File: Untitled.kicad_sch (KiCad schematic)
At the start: 11 parts, among them K1 Fujitsu_FTR-LYAA005x, Q2 IRLB8721PBF, Q3 IRLB8721PBF, Q4 IRLB8721PBF, U1 ESP32-S3, U3 LSM6DS3, U4 MS5611-01BA

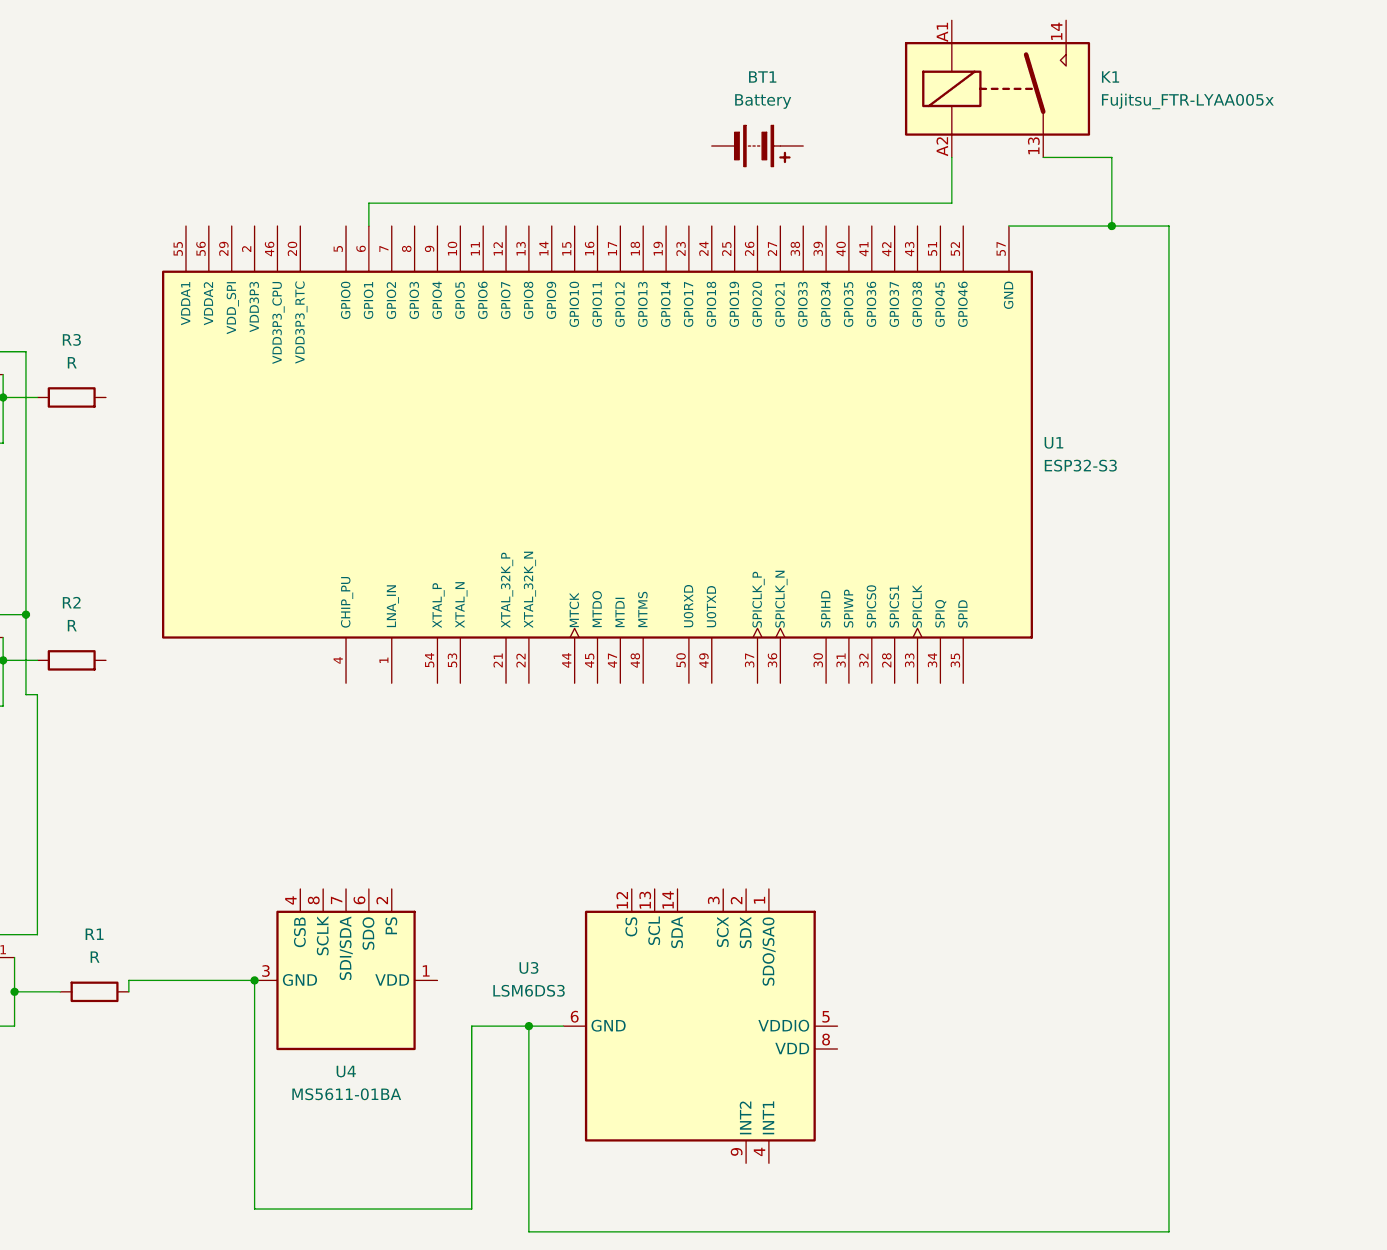
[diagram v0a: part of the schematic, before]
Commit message: Added Correct Microcontroller
Add the correct symbol for the microcontroller library
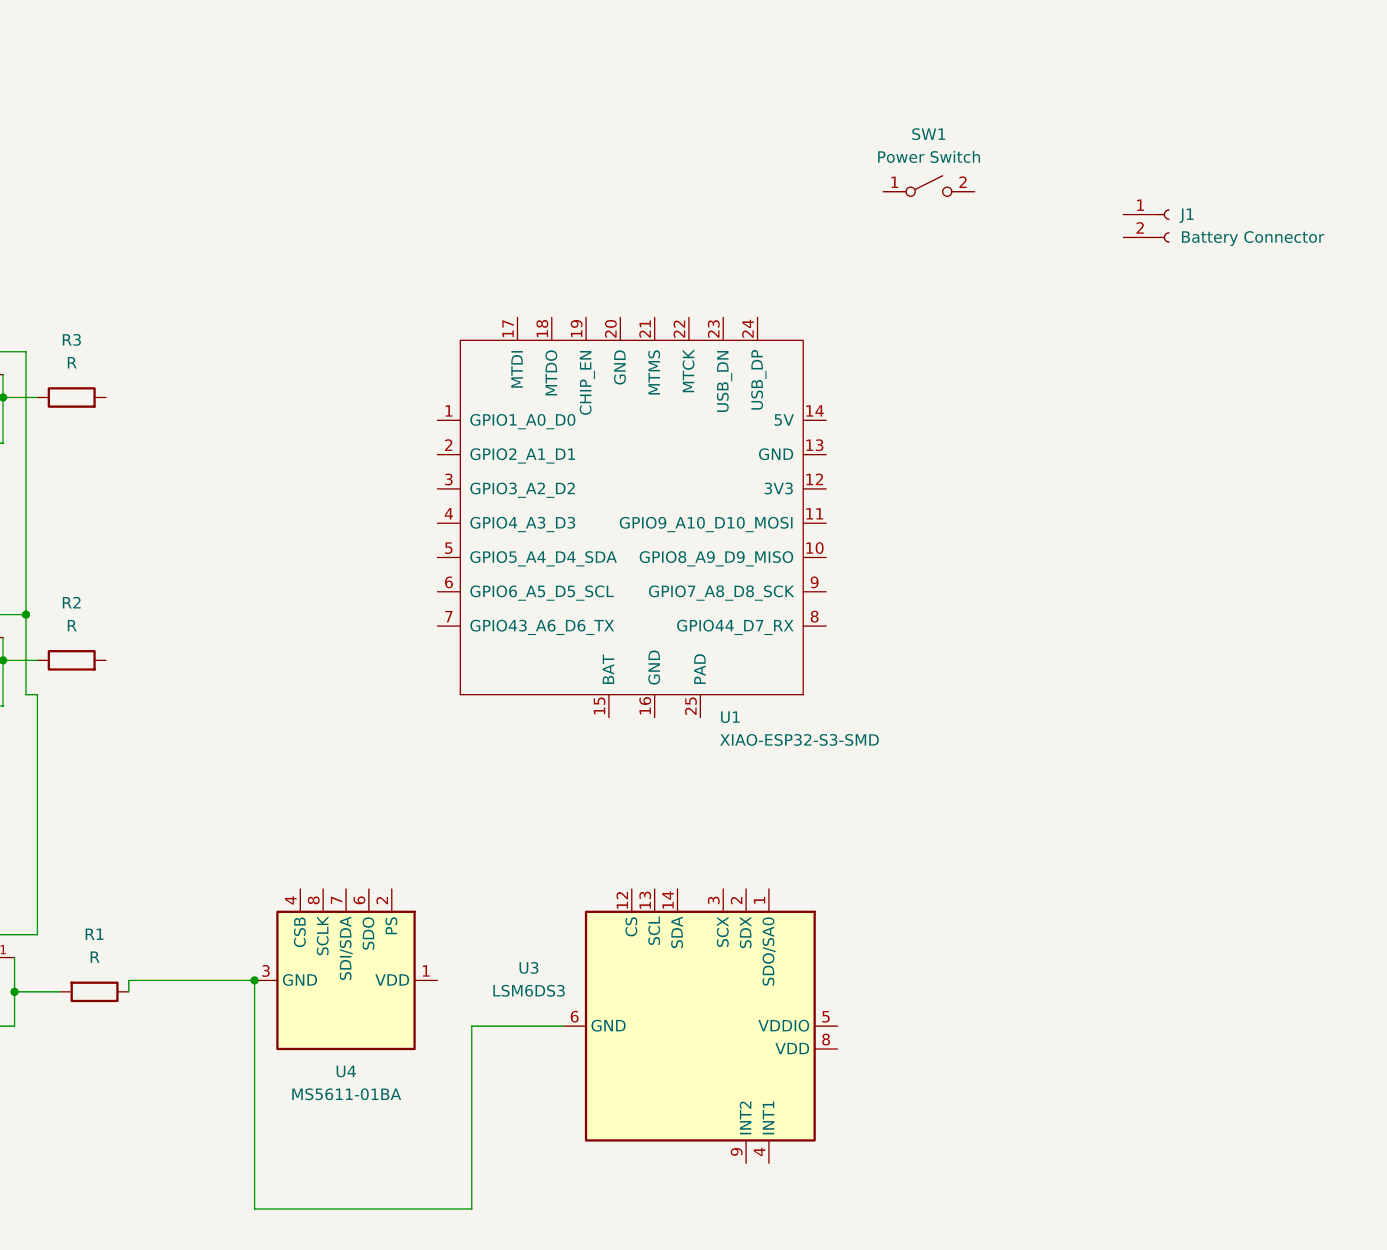
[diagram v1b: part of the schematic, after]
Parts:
- removed BT1: Battery, symbol Device:Battery
- removed K1: Fujitsu_FTR-LYAA005x, Relay_THT:Relay_SPST-NO_Fujitsu_FTR-LYAA005x_FormA_Vertical, symbol Relay:Fujitsu_FTR-LYAA005x
- removed U1: ESP32-S3, ESP32-S3:IC_ESP32-S3, symbol ESP32-S3:ESP32-S3
- added J1: Battery Connector, symbol Connector:Conn_01x02_Socket
- added SW1: Power Switch, symbol Switch:SW_SPST
- added U1: XIAO-ESP32-S3-SMD, symbol SeeedStudio-XIAO:XIAO-ESP32-S3-SMD

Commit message: Fixed Microcontroller Library
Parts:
- added C1, C2, C3: 100nF, symbol Device:C_US
- added R4, R5: 10K, symbol Device:R_US
- U1: footprint (none) -> Seeed Studio XIAO Series Library:XIAO-ESP32S3-DIP
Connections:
- net at U4.1 (VDD): now also U1.12 (3V3), U3.5 (VDDIO), U3.8 (VDD), U4.2 (PS), C1.1, C2.2, C3.1, R4.1, R5.1
- net at R1.1, U3.6 (GND), U3.7 (GND)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: now also U1.13 (GND), C1.2, C2.1, C3.2
- net at U4.7 (SDI/SDA): now also U1.5 (GPIO5_A4_D4_SDA), R4.2
- net at U4.8 (SCLK): now also U1.6 (GPIO6_A5_D5_SCL), R5.2

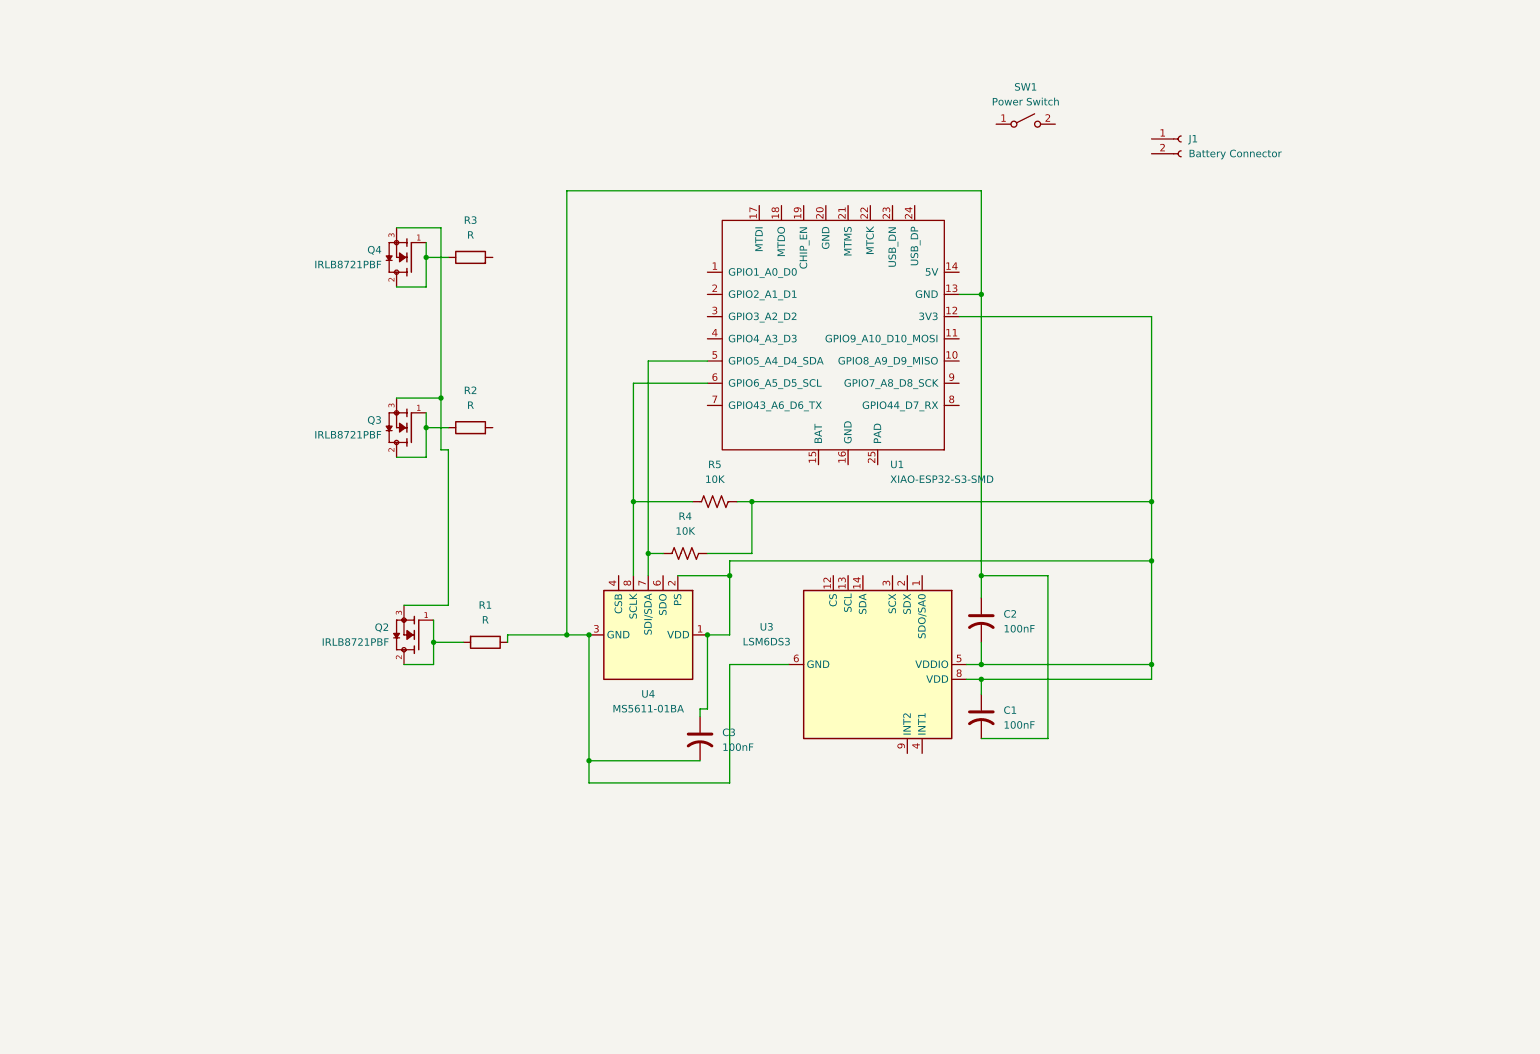
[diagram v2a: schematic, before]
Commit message: Sensor Wiring Finished
Finished the wiring for both sensors. Cleaned up diagram by using net labels rather than directly connecting everything. Left MOSTFETs unfinished bc they will likely be on a separate board.
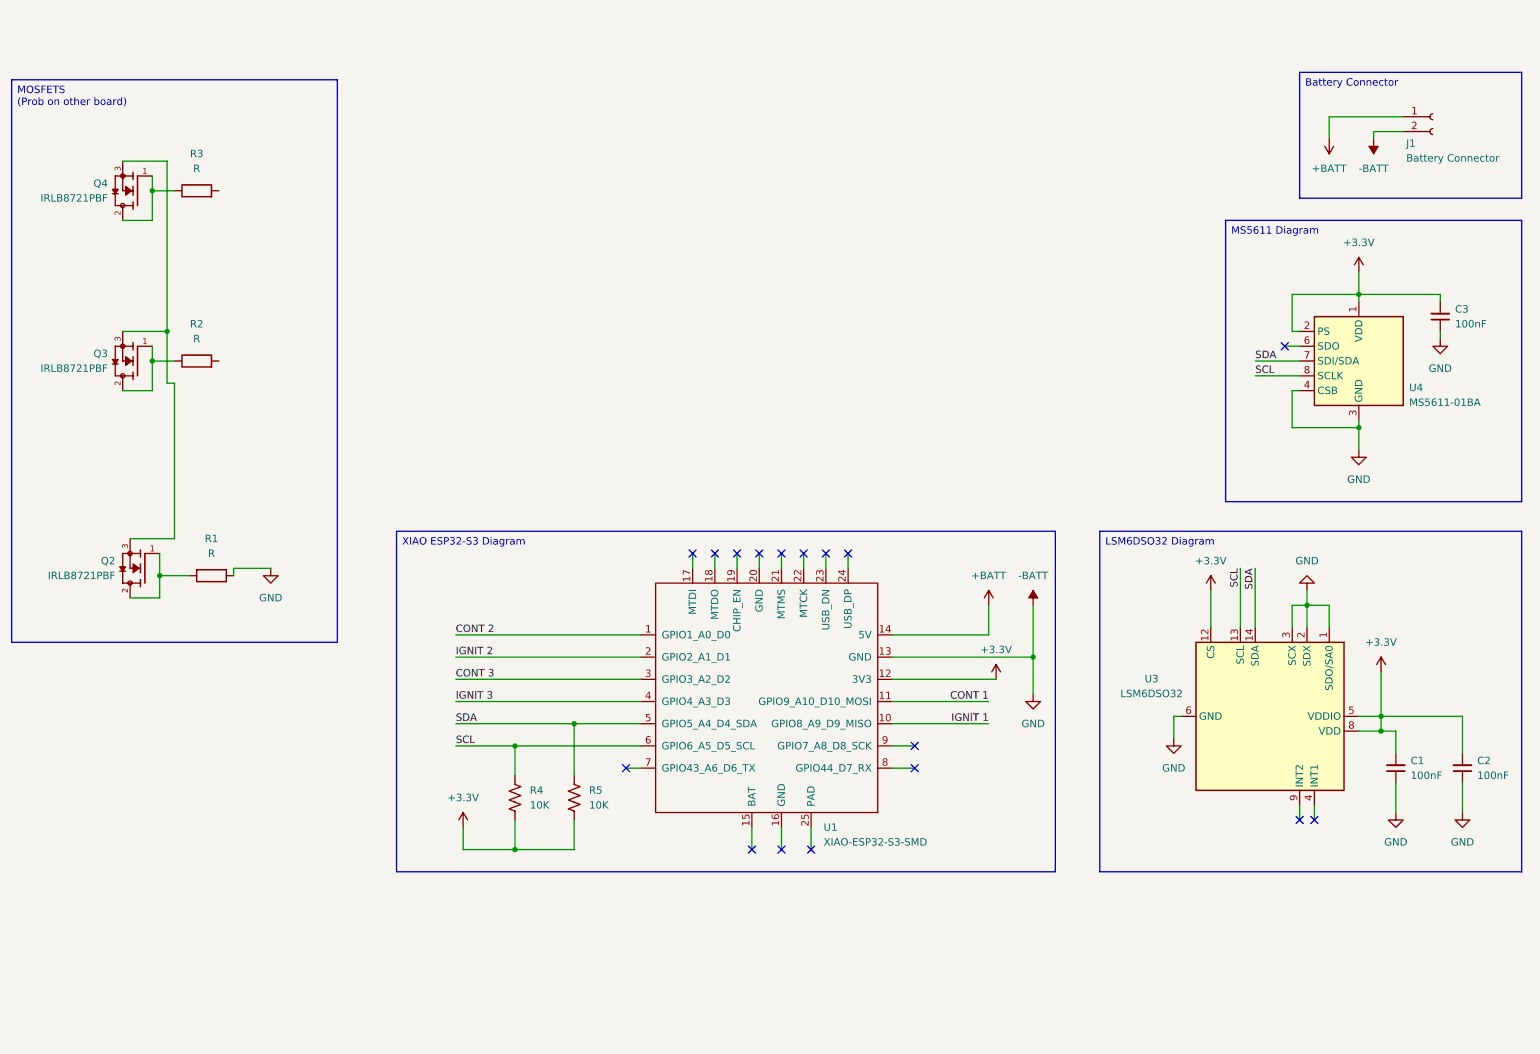
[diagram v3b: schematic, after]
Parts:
- removed C1, C2, C3: 100nF, symbol Device:C_US
- removed SW1: Power Switch, symbol Switch:SW_SPST
- added C1, C2, C3: 100nF, symbol Device:C_Small
- U3: value LSM6DS3 -> LSM6DSO32
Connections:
- net +3.3V: now reaches U1.12 (3V3), U3.5 (VDDIO), U3.8 (VDD), U4.1 (VDD), U4.2 (PS)
- net +3.3V: now also R4.2, R5.2, U3.12 (CS), C1.2, C2.2, C3.2; no longer R4.1, R5.1
- net -BATT: now reaches R1.1, U1.13 (GND), U3.6 (GND), U3.7 (GND), U4.3 (GND)
- net -BATT: now also J1.2 (Pin_2), U3.1 (SDO/SA0), U3.2 (SDX), U3.3 (SCX), U4.4 (CSB), U4.5 (CSB), C1.1, C2.1, C3.1
- net SDA: now reaches U1.5 (GPIO5_A4_D4_SDA), U4.7 (SDI/SDA)
- net SDA: now also R5.1, U3.14 (SDA); no longer R4.2
- net SCL: now reaches U1.6 (GPIO6_A5_D5_SCL), U4.8 (SCLK)
- net SCL: now also R4.1, U3.13 (SCL); no longer R5.2
- net CONT 2: now reaches U1.1 (GPIO1_A0_D0)
- net IGNIT 1: now reaches U1.10 (GPIO8_A9_D9_MISO)
- net CONT 1: now reaches U1.11 (GPIO9_A10_D10_MOSI)
- net +BATT: now reaches U1.14 (5V)
- net +BATT: now also J1.1 (Pin_1)
- net IGNIT 2: now reaches U1.2 (GPIO2_A1_D1)
- net CONT 3: now reaches U1.3 (GPIO3_A2_D2)
- net IGNIT 3: now reaches U1.4 (GPIO4_A3_D3)
- no-connect marks 0 -> 17
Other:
- company: (none) -> UC Rocketry Club
- title: (none) -> Custom Avionics (Sensor Layer)
- moved on the sheet: J1, Q2, Q3, Q4, R1, R2, R3, R4, R5, U1, U3, U4

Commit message: Finished Schematic & Assigned Footprints
Finished up the schematic, making this version applicable to the entire system rather than a single layer. Assigned footprints for every schematic component, did some very basic layout in the schematic editor.
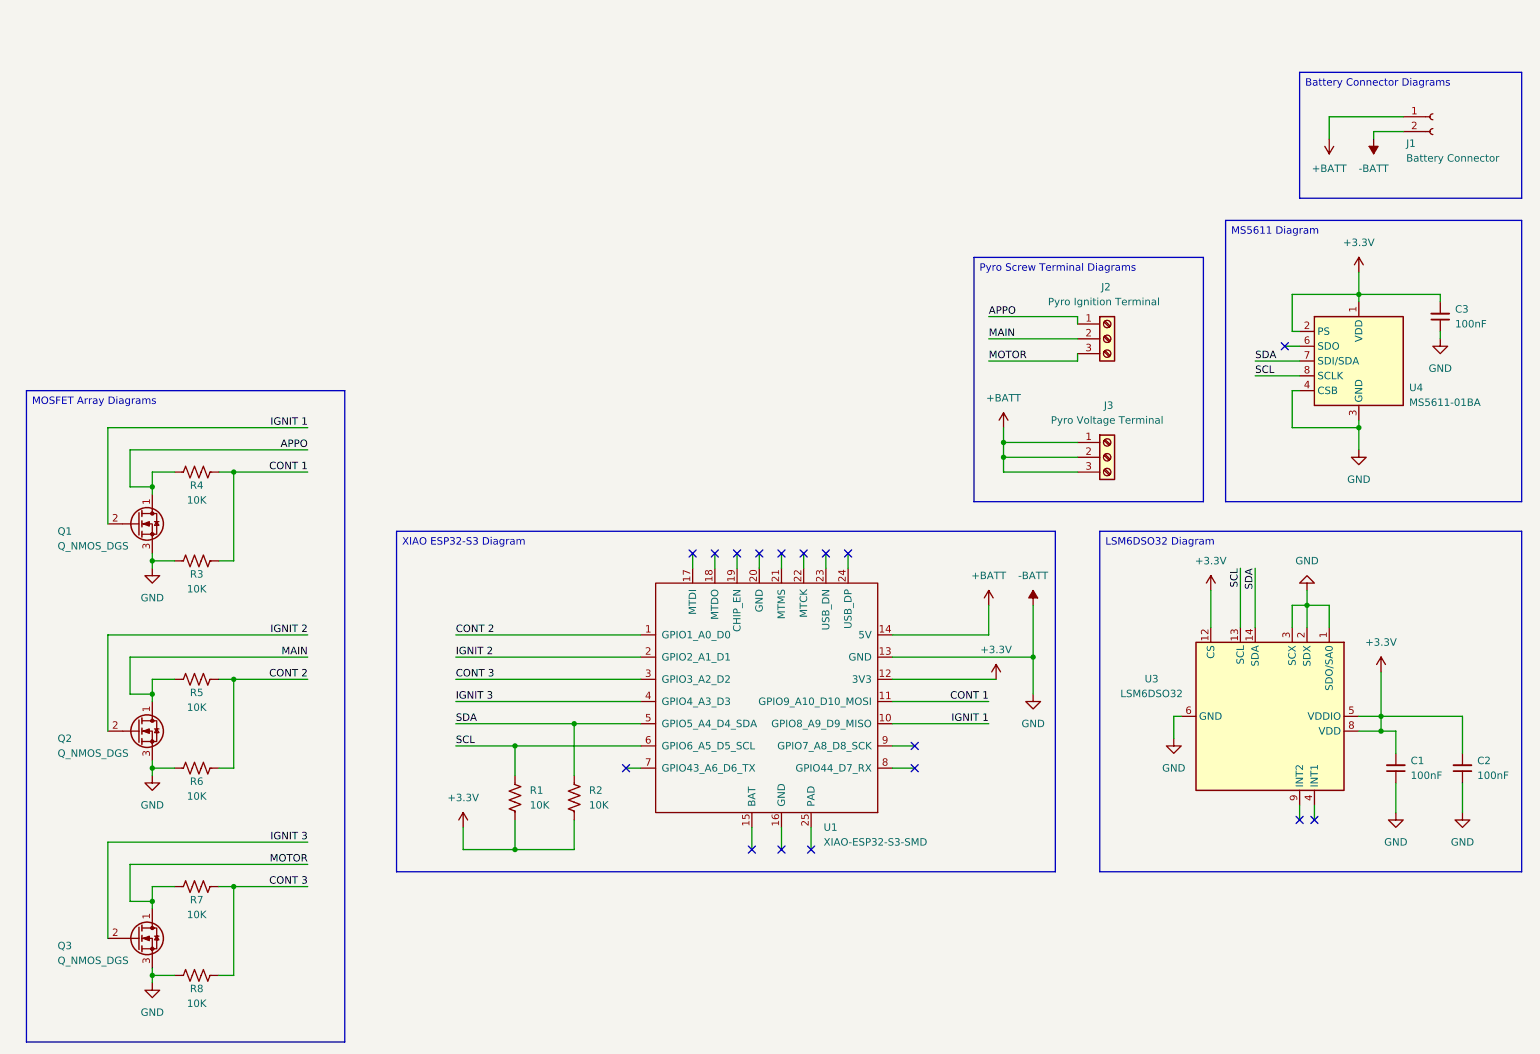
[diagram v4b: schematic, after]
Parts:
- removed Q2, Q3, Q4: IRLB8721PBF, IRLB8721PBF:TO254P1067X483X2057-3, symbol IRLB8721PBF:IRLB8721PBF
- removed R1, R2, R3: R, symbol Device:R
- added J2: Pyro Ignition Terminal, TerminalBlock_Phoenix:TerminalBlock_Phoenix_MKDS-1,5-3-5.08_1x03_P5.08mm_Horizontal, symbol Connector:Screw_Terminal_01x03
- added J3: Pyro Voltage Terminal, TerminalBlock_Phoenix:TerminalBlock_Phoenix_MKDS-1,5-3-5.08_1x03_P5.08mm_Horizontal, symbol Connector:Screw_Terminal_01x03
- added Q1, Q2, Q3: Q_NMOS_DGS, Package_TO_SOT_SMD:TSOT-23, symbol Transistor_FET:Q_NMOS_DGS
- added R3, R4, R5, R6, R7, R8: 10K, Resistor_SMD:R_0805_2012Metric_Pad1.20x1.40mm_HandSolder, symbol Device:R_US
- C1, C2, C3: footprint (none) -> Capacitor_SMD:C_0805_2012Metric_Pad1.18x1.45mm_HandSolder
- J1: footprint (none) -> Connector_JST:JST_PH_B2B-PH-K_1x02_P2.00mm_Vertical
- R1: renamed from R4; footprint (none) -> Resistor_SMD:R_0805_2012Metric_Pad1.20x1.40mm_HandSolder
- R2: renamed from R5; footprint (none) -> Resistor_SMD:R_0805_2012Metric_Pad1.20x1.40mm_HandSolder
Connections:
- net +BATT: now also J3.1 (Pin_1), J3.2 (Pin_2), J3.3 (Pin_3)
- net -BATT: now also Q1.3 (S), Q2.3 (S), Q3.3 (S), R3.2, R6.2, R8.2
- net CONT 1: now also R3.1, R4.1
- net CONT 2: now also R5.1, R6.1
- net CONT 3: now also R7.1, R8.1
- net IGNIT 1: now also Q1.2 (G)
- net IGNIT 2: now also Q2.2 (G)
- net IGNIT 3: now also Q3.2 (G)
- new net APPO: J2.1 (Pin_1), Q1.1 (D), R4.2
- new net MAIN: J2.2 (Pin_2), Q2.1 (D), R5.2
- new net MOTOR: J2.3 (Pin_3), Q3.1 (D), R7.2
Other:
- title: Custom Avionics (Sensor Layer) -> Custom Avionics (All Layers)
